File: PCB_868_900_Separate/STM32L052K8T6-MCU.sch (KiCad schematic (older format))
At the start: 27 parts, among them J2 20021121-00010C4LF, J3 B4B-PH-K-S(LF)(SN), J5 0475890001-MicroUSBPort, P1 CONN_02X03, SW2 B3U-1000P, U3 STM32L052C8T6, X3 ABM10-166-12.000MHZ-T3

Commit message: License added and dedicated PA/LNA Match
Working on the separate PA/LNA match version. also added cern license
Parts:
- removed J3: B4B-PH-K-S(LF)(SN), PCB_Footprints:B4B-PH-K-S(LF)(SN), symbol B4B-PH-K-S(LF)(SN)
- removed P1: CONN_02X03, Pin_Headers:Pin_Header_Straight_2x03, symbol CONN_02X03
- added P1: CONN_02X08, Pin_Headers:Pin_Header_Straight_2x08, symbol CONN_02X08
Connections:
- net labels added: PSU_IN, VIN
- wire segments 74 -> 76
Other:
- moved on the sheet: LED2, LED3, R7, R8

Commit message: PCBs Tweaked A lot
PCBs have been tweaked. The separate implementation has been finished
but also has GPIOs from the MCU broken out to the connector, same for
the combined implementation. Both boards now have power indication LEDs
(red).
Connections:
- net labels added: GPIO_PA8, GPIO_PB0, GPIO_PB1, GPIO_PB10, GPIO_PB11, GPIO_PB2
- wire segments 76 -> 88
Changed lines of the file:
@@
 $EndComp
 $Comp
-L GND #PWR30
+L GND #PWR32
 U 1 1 582190B8
 P 1400 5050
-F 0 "#PWR30" H 1400 4800 50  0001 C CNN
+F 0 "#PWR32" H 1400 4800 50  0001 C CNN
 F 1 "GND" H 1405 4877 50  0000 C CNN
 F 2 "" H 1400 5050 50  0000 C CNN
@@
 $EndComp
 $Comp
-L GND #PWR40
+L GND #PWR42
 U 1 1 58219186
 P 4750 5800
-F 0 "#PWR40" H 4750 5550 50  0001 C CNN
+F 0 "#PWR42" H 4750 5550 50  0001 C CNN
 F 1 "GND" H 4755 5627 50  0000 C CNN
 F 2 "" H 4750 5800 50  0000 C CNN
@@
 $EndComp
 $Comp
-L +3.3V #PWR29
+L +3.3V #PWR31
 U 1 1 58219330
 P 1400 4000
-F 0 "#PWR29" H 1400 3850 50  0001 C CNN
+F 0 "#PWR31" H 1400 3850 50  0001 C CNN
 F 1 "+3.3V" H 1415 4173 50  0000 C CNN
 F 2 "" H 1400 4000 50  0000 C CNN
@@
 $EndComp
 $Comp
-L GND #PWR38
+L GND #PWR40
 U 1 1 58219BE3
 P 3450 2950
-F 0 "#PWR38" H 3450 2700 50  0001 C CNN
+F 0 "#PWR40" H 3450 2700 50  0001 C CNN
 F 1 "GND" H 3455 2777 50  0000 C CNN
 F 2 "" H 3450 2950 50  0000 C CNN
@@
 $EndComp
 $Comp
-L +3.3V #PWR36
+L +3.3V #PWR38
 U 1 1 58219CF5
 P 3100 2500
-F 0 "#PWR36" H 3100 2350 50  0001 C CNN
+F 0 "#PWR38" H 3100 2350 50  0001 C CNN
 F 1 "+3.3V" H 3115 2673 50  0000 C CNN
 F 2 "" H 3100 2500 50  0000 C CNN
@@
 $EndComp
 $Comp
-L GND #PWR34
+L GND #PWR36
 U 1 1 5821A196
 P 1700 2950
-F 0 "#PWR34" H 1700 2700 50  0001 C CNN
+F 0 "#PWR36" H 1700 2700 50  0001 C CNN
 F 1 "GND" H 1705 2777 50  0000 C CNN
 F 2 "" H 1700 2950 50  0000 C CNN
@@
 $EndComp
 $Comp
-L GND #PWR35
+L GND #PWR37
 U 1 1 5821A1E0
 P 2500 2950
-F 0 "#PWR35" H 2500 2700 50  0001 C CNN
+F 0 "#PWR37" H 2500 2700 50  0001 C CNN
 F 1 "GND" H 2505 2777 50  0000 C CNN
 F 2 "" H 2500 2950 50  0000 C CNN
@@
 $EndComp
 $Comp
-L +3.3V #PWR33
+L +3.3V #PWR35
 U 1 1 5821A692
 P 1500 2500
-F 0 "#PWR33" H 1500 2350 50  0001 C CNN
+F 0 "#PWR35" H 1500 2350 50  0001 C CNN
 F 1 "+3.3V" H 1515 2673 50  0000 C CNN
 F 2 "" H 1500 2500 50  0000 C CNN
@@
 $EndComp
 $Comp
-L GND #PWR46
+L GND #PWR48
 U 1 1 58221381
 P 9975 3900
-F 0 "#PWR46" H 9975 3650 50  0001 C CNN
+F 0 "#PWR48" H 9975 3650 50  0001 C CNN
 F 1 "GND" H 9980 3727 50  0000 C CNN
 F 2 "" H 9975 3900 50  0000 C CNN
@@
 $EndComp
 $Comp
-L GND #PWR48
+L GND #PWR50
 U 1 1 58221B76
 P 10475 4775
-F 0 "#PWR48" H 10475 4525 50  0001 C CNN
+F 0 "#PWR50" H 10475 4525 50  0001 C CNN
 F 1 "GND" H 10480 4602 50  0000 C CNN
 F 2 "" H 10475 4775 50  0000 C CNN
@@
 $EndComp
 $Comp
-L GND #PWR45
+L GND #PWR47
 U 1 1 58223B2D
 P 9600 4775
-F 0 "#PWR45" H 9600 4525 50  0001 C CNN
+F 0 "#PWR47" H 9600 4525 50  0001 C CNN
 F 1 "GND" H 9605 4602 50  0000 C CNN
 F 2 "" H 9600 4775 50  0000 C CNN
@@
 $EndComp
 $Comp
-L GND #PWR44
+L GND #PWR46
 U 1 1 58224185
 P 9050 4375
-F 0 "#PWR44" H 9050 4125 50  0001 C CNN
+F 0 "#PWR46" H 9050 4125 50  0001 C CNN
 F 1 "GND" H 9055 4202 50  0000 C CNN
 F 2 "" H 9050 4375 50  0000 C CNN
@@
 $EndComp
 $Comp
-L GND #PWR47
+L GND #PWR49
 U 1 1 58224D2B
 P 10425 3125
-F 0 "#PWR47" H 10425 2875 50  0001 C CNN
+F 0 "#PWR49" H 10425 2875 50  0001 C CNN
 F 1 "GND" H 10430 2952 50  0000 C CNN
 F 2 "" H 10425 3125 50  0000 C CNN
@@
 U 1 1 58226A3F
 P 7900 5750
-F 0 "LED2" V 7800 4775 60  0000 L CNN
-F 1 "LTST-C193TBKT-5A" V 7900 4775 60  0000 L CNN
+F 0 "LED2" V 7950 4700 60  0000 L CNN
+F 1 "LTST-C193TBKT-5A" V 8050 4700 60  0000 L CNN
 F 2 "PCB_Footprints:LED0603" H 9325 7675 60  0001 C CNN
 F 3 "http://optoelectronics.liteon.com/upload/download/DS22-2004-060/P_100_LTST-C193TBKT-5A.pdf" H 9525 7800 60  0001 C CNN
@@
 NRST
 $Comp
-L GND #PWR32
+L GND #PWR34
 U 1 1 5824BA14
 P 1400 6250
-F 0 "#PWR32" H 1400 6000 50  0001 C CNN
+F 0 "#PWR34" H 1400 6000 50  0001 C CNN
 F 1 "GND" H 1405 6077 50  0000 C CNN
 F 2 "" H 1400 6250 50  0000 C CNN
@@
 $EndComp
 $Comp
-L +3.3V #PWR31
+L +3.3V #PWR33
 U 1 1 5824BBC1
 P 1400 5575
-F 0 "#PWR31" H 1400 5425 50  0001 C CNN
+F 0 "#PWR33" H 1400 5425 50  0001 C CNN
 F 1 "+3.3V" H 1415 5748 50  0000 C CNN
 F 2 "" H 1400 5575 50  0000 C CNN
@@
 $EndComp
 $Comp
-L GND #PWR43
+L GND #PWR45
 U 1 1 58250111
 P 8025 6000
-F 0 "#PWR43" H 8025 5750 50  0001 C CNN
+F 0 "#PWR45" H 8025 5750 50  0001 C CNN
 F 1 "GND" H 8030 5827 50  0000 C CNN
 F 2 "" H 8025 6000 50  0000 C CNN
@@
 $EndComp
 $Comp
-L GND #PWR39
+L GND #PWR41
 U 1 1 582650D6
 P 4150 4375
-F 0 "#PWR39" H 4150 4125 50  0001 C CNN
+F 0 "#PWR41" H 4150 4125 50  0001 C CNN
 F 1 "GND" H 4155 4202 50  0000 C CNN
 F 2 "" H 4150 4375 50  0000 C CNN
@@
 Connection ~ 3250 4200
 $Comp
-L GND #PWR37
+L GND #PWR39
 U 1 1 58299A73
 P 3125 4200
-F 0 "#PWR37" H 3125 3950 50  0001 C CNN
+F 0 "#PWR39" H 3125 3950 50  0001 C CNN
 F 1 "GND" H 3130 4027 50  0000 C CNN
 F 2 "" H 3125 4200 50  0000 C CNN
@@
 F 3 "" H 5575 5625 50  0000 C CNN
 	1    5575 6825
-	1    0    0    -1
-$EndComp
-Text Label 6000 6975 0    60   ~ 0
+	-1   0    0    1
+$EndComp
+Text Label 5900 6975 0    60   ~ 0
 USART1_TX
-Text Label 6000 6875 0    60   ~ 0
+Text Label 4850 6975 0    60   ~ 0
 USART1_RX
 Wire Wire Line
 	5825 6975 6625 6975
 Wire Wire Line
-	5825 6875 6625 6875
-Text Label 5950 6775 0    60   ~ 0
+	4525 6975 5325 6975
+Text Label 4850 6575 0    60   ~ 0
 SPI2_MOSI
-Text Label 5925 6675 0    60   ~ 0
+Text Label 5875 6575 0    60   ~ 0
 SPI2_MISO
-Text Label 5925 6575 0    60   ~ 0
+Text Label 4850 6475 0    60   ~ 0
 SPI2_SCLK
-Text Label 5925 6475 0    60   ~ 0
+Text Label 5875 6475 0    60   ~ 0
 SPI2_NSS
 Wire Wire Line
-	6400 6775 5825 6775
+	5325 6575 4750 6575
+Wire Wire Line
+	4750 6475 5325 6475
+Wire Wire Line
+	5825 6475 6400 6475
 Wire Wire Line
 	5825 6575 6400 6575
-Wire Wire Line
-	5825 6475 6400 6475
-Wire Wire Line
-	5825 6675 6400 6675
 Text HLabel 10975 5250 2    60   Input ~ 0
 VIN
@@
 Text Label 10300 5250 0    60   ~ 0
 PSU_IN
-Text Label 5950 7075 0    60   ~ 0
+Text Label 5000 7175 0    60   ~ 0
 PSU_IN
 Wire Wire Line
-	6400 7075 5825 7075
-$Comp
-L GND #PWR42
+	5325 7175 4750 7175
+$Comp
+L GND #PWR44
 U 1 1 58246BF1
 P 5825 7175
-F 0 "#PWR42" H 5825 6925 50  0001 C CNN
+F 0 "#PWR44" H 5825 6925 50  0001 C CNN
 F 1 "GND" H 5830 7002 50  0000 C CNN
 F 2 "" H 5825 7175 50  0000 C CNN
@@
 $EndComp
 $Comp
-L GND #PWR41
+L GND #PWR43
 U 1 1 5824B1D0
-P 5325 7175
-F 0 "#PWR41" H 5325 6925 50  0001 C CNN
-F 1 "GND" H 5330 7002 50  0000 C CNN
-F 2 "" H 5325 7175 50  0000 C CNN
-F 3 "" H 5325 7175 50  0000 C CNN
-	1    5325 7175
-	1    0    0    -1
-$EndComp
+P 4700 7400
+F 0 "#PWR43" H 4700 7150 50  0001 C CNN
+F 1 "GND" H 4705 7227 50  0000 C CNN
+F 2 "" H 4700 7400 50  0000 C CNN
+F 3 "" H 4700 7400 50  0000 C CNN
+	1    4700 7400
+	1    0    0    -1
+$EndComp
+Text Label 6500 4200 0    60   ~ 0
+GPIO_PB0
+Text Label 6500 4300 0    60   ~ 0
+GPIO_PB1
+Text Label 6500 4400 0    60   ~ 0
+GPIO_PB2
+Text Label 6500 5200 0    60   ~ 0
+GPIO_PB10
+Text Label 6500 5300 0    60   ~ 0
+GPIO_PB11
+Wire Wire Line
+	7050 5200 6500 5200
+Wire Wire Line
+	7050 5300 6500 5300
+Wire Wire Line
+	7025 4400 6500 4400
+Wire Wire Line
+	7025 4300 6500 4300
+Wire Wire Line
+	7025 4200 6500 4200
+Text Label 5875 6675 0    60   ~ 0
+GPIO_PB0
+Text Label 4850 6675 0    60   ~ 0
+GPIO_PB1
+Text Label 5875 6775 0    60   ~ 0
+GPIO_PB2
+Wire Wire Line
+	6350 6775 5825 6775
+Wire Wire Line
+	5325 6675 4800 6675
+Wire Wire Line
+	6350 6675 5825 6675
+Text Label 4850 6775 0    60   ~ 0
+GPIO_PB10
+Text Label 5875 6875 0    60   ~ 0
+GPIO_PB11
+Wire Wire Line
+	5325 6775 4775 6775
+Wire Wire Line
+	6375 6875 5825 6875
+Wire Wire Line
+	6500 3300 7225 3300
+Text Label 6650 3300 0    60   ~ 0
+GPIO_PA8
+Text Label 4850 6875 0    60   ~ 0
+GPIO_PA8
+Wire Wire Line
+	5325 6875 4775 6875
 $EndSCHEMATC

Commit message: Additional GPIO
Two additional GPIO pins from the STM32L0 have been added to the
connector, now there is a signal on every pin. The connector component
has been replaced with one that has a STEP 3D model for proper 3D model
exporting from KiCAD for enclosure design. This has been done to both
versions of the radio.
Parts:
- removed P1: CONN_02X08, Pin_Headers:Pin_Header_Straight_2x08, symbol CONN_02X08
- added P1: 61301621121, PCB_Footprints:61301621121, symbol 61301621121
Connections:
- net labels added: GPIO_PA15, GPIO_PB3
- wire segments 88 -> 92
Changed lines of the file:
@@
 $EndComp
 $Comp
-L GND #PWR33
+L GND #PWR032
 U 1 1 582190B8
 P 1400 5050
-F 0 "#PWR33" H 1400 4800 50  0001 C CNN
+F 0 "#PWR032" H 1400 4800 50  0001 C CNN
 F 1 "GND" H 1405 4877 50  0000 C CNN
 F 2 "" H 1400 5050 50  0000 C CNN
@@
 $EndComp
 $Comp
-L GND #PWR44
+L GND #PWR033
 U 1 1 58219186
 P 4750 5800
-F 0 "#PWR44" H 4750 5550 50  0001 C CNN
+F 0 "#PWR033" H 4750 5550 50  0001 C CNN
 F 1 "GND" H 4755 5627 50  0000 C CNN
 F 2 "" H 4750 5800 50  0000 C CNN
@@
 $EndComp
 $Comp
-L +3.3V #PWR32
+L +3.3V #PWR034
 U 1 1 58219330
 P 1400 4000
-F 0 "#PWR32" H 1400 3850 50  0001 C CNN
+F 0 "#PWR034" H 1400 3850 50  0001 C CNN
 F 1 "+3.3V" H 1415 4173 50  0000 C CNN
 F 2 "" H 1400 4000 50  0000 C CNN
@@
 $EndComp
 $Comp
-L GND #PWR41
+L GND #PWR035
 U 1 1 58219BE3
 P 3450 2950
-F 0 "#PWR41" H 3450 2700 50  0001 C CNN
+F 0 "#PWR035" H 3450 2700 50  0001 C CNN
 F 1 "GND" H 3455 2777 50  0000 C CNN
 F 2 "" H 3450 2950 50  0000 C CNN
@@
 $EndComp
 $Comp
-L +3.3V #PWR39
+L +3.3V #PWR036
 U 1 1 58219CF5
 P 3100 2500
-F 0 "#PWR39" H 3100 2350 50  0001 C CNN
+F 0 "#PWR036" H 3100 2350 50  0001 C CNN
 F 1 "+3.3V" H 3115 2673 50  0000 C CNN
 F 2 "" H 3100 2500 50  0000 C CNN
@@
 $EndComp
 $Comp
-L GND #PWR37
+L GND #PWR037
 U 1 1 5821A196
 P 1700 2950
-F 0 "#PWR37" H 1700 2700 50  0001 C CNN
+F 0 "#PWR037" H 1700 2700 50  0001 C CNN
 F 1 "GND" H 1705 2777 50  0000 C CNN
 F 2 "" H 1700 2950 50  0000 C CNN
@@
 $EndComp
 $Comp
-L GND #PWR38
+L GND #PWR038
 U 1 1 5821A1E0
 P 2500 2950
-F 0 "#PWR38" H 2500 2700 50  0001 C CNN
+F 0 "#PWR038" H 2500 2700 50  0001 C CNN
 F 1 "GND" H 2505 2777 50  0000 C CNN
 F 2 "" H 2500 2950 50  0000 C CNN
@@
 $EndComp
 $Comp
-L +3.3V #PWR36
+L +3.3V #PWR039
 U 1 1 5821A692
 P 1500 2500
-F 0 "#PWR36" H 1500 2350 50  0001 C CNN
+F 0 "#PWR039" H 1500 2350 50  0001 C CNN
 F 1 "+3.3V" H 1515 2673 50  0000 C CNN
 F 2 "" H 1500 2500 50  0000 C CNN
@@
 $EndComp
 $Comp
-L GND #PWR49
+L GND #PWR040
 U 1 1 58221381
 P 9975 3900
-F 0 "#PWR49" H 9975 3650 50  0001 C CNN
+F 0 "#PWR040" H 9975 3650 50  0001 C CNN
 F 1 "GND" H 9980 3727 50  0000 C CNN
 F 2 "" H 9975 3900 50  0000 C CNN
@@
 $EndComp
 $Comp
-L GND #PWR51
+L GND #PWR041
 U 1 1 58221B76
 P 10475 4775
-F 0 "#PWR51" H 10475 4525 50  0001 C CNN
+F 0 "#PWR041" H 10475 4525 50  0001 C CNN
 F 1 "GND" H 10480 4602 50  0000 C CNN
 F 2 "" H 10475 4775 50  0000 C CNN
@@
 $EndComp
 $Comp
-L GND #PWR48
+L GND #PWR042
 U 1 1 58223B2D
 P 9600 4775
-F 0 "#PWR48" H 9600 4525 50  0001 C CNN
+F 0 "#PWR042" H 9600 4525 50  0001 C CNN
 F 1 "GND" H 9605 4602 50  0000 C CNN
 F 2 "" H 9600 4775 50  0000 C CNN
@@
 $EndComp
 $Comp
-L GND #PWR47
+L GND #PWR043
 U 1 1 58224185
 P 9050 4375
-F 0 "#PWR47" H 9050 4125 50  0001 C CNN
+F 0 "#PWR043" H 9050 4125 50  0001 C CNN
 F 1 "GND" H 9055 4202 50  0000 C CNN
 F 2 "" H 9050 4375 50  0000 C CNN
@@
 $EndComp
 $Comp
-L GND #PWR50
+L GND #PWR044
 U 1 1 58224D2B
 P 10425 3125
-F 0 "#PWR50" H 10425 2875 50  0001 C CNN
+F 0 "#PWR044" H 10425 2875 50  0001 C CNN
 F 1 "GND" H 10430 2952 50  0000 C CNN
 F 2 "" H 10425 3125 50  0000 C CNN
@@
 NRST
 $Comp
-L GND #PWR35
+L GND #PWR045
 U 1 1 5824BA14
 P 1400 6250
-F 0 "#PWR35" H 1400 6000 50  0001 C CNN
+F 0 "#PWR045" H 1400 6000 50  0001 C CNN
 F 1 "GND" H 1405 6077 50  0000 C CNN
 F 2 "" H 1400 6250 50  0000 C CNN
@@
 $EndComp
 $Comp
-L +3.3V #PWR34
+L +3.3V #PWR046
 U 1 1 5824BBC1
 P 1400 5575
-F 0 "#PWR34" H 1400 5425 50  0001 C CNN
+F 0 "#PWR046" H 1400 5425 50  0001 C CNN
 F 1 "+3.3V" H 1415 5748 50  0000 C CNN
 F 2 "" H 1400 5575 50  0000 C CNN
@@
 $EndComp
 $Comp
-L GND #PWR46
+L GND #PWR047
 U 1 1 58250111
 P 8025 6000
-F 0 "#PWR46" H 8025 5750 50  0001 C CNN
+F 0 "#PWR047" H 8025 5750 50  0001 C CNN
 F 1 "GND" H 8030 5827 50  0000 C CNN
 F 2 "" H 8025 6000 50  0000 C CNN
@@
 $EndComp
 $Comp
-L GND #PWR42
+L GND #PWR048
 U 1 1 582650D6
 P 4150 4375
-F 0 "#PWR42" H 4150 4125 50  0001 C CNN
+F 0 "#PWR048" H 4150 4125 50  0001 C CNN
 F 1 "GND" H 4155 4202 50  0000 C CNN
 F 2 "" H 4150 4375 50  0000 C CNN
@@
 Connection ~ 3250 4200
 $Comp
-L GND #PWR40
+L GND #PWR049
 U 1 1 58299A73
 P 3125 4200
-F 0 "#PWR40" H 3125 3950 50  0001 C CNN
+F 0 "#PWR049" H 3125 3950 50  0001 C CNN
 F 1 "GND" H 3130 4027 50  0000 C CNN
 F 2 "" H 3125 4200 50  0000 C CNN
@@
 $EndComp
 Connection ~ 3125 4200
-$Comp
-L CONN_02X08 P1
-U 1 1 5823F6D4
-P 5575 6825
-F 0 "P1" H 5575 7390 50  0000 C CNN
-F 1 "CONN_02X08" H 5575 7299 50  0000 C CNN
-F 2 "Pin_Headers:Pin_Header_Straight_2x08" H 5575 5625 50  0001 C CNN
-F 3 "" H 5575 5625 50  0000 C CNN
-	1    5575 6825
-	-1   0    0    1
-$EndComp
-Text Label 5900 6975 0    60   ~ 0
+Text Label 6000 6975 0    60   ~ 0
 USART1_TX
 Text Label 4850 6975 0    60   ~ 0
 USART1_RX
 Wire Wire Line
-	5825 6975 6625 6975
+	5925 6975 6725 6975
 Wire Wire Line
 	4525 6975 5325 6975
 Text Label 4850 6575 0    60   ~ 0
 SPI2_MOSI
-Text Label 5875 6575 0    60   ~ 0
+Text Label 5975 6575 0    60   ~ 0
 SPI2_MISO
 Text Label 4850 6475 0    60   ~ 0
 SPI2_SCLK
-Text Label 5875 6475 0    60   ~ 0
+Text Label 5975 6475 0    60   ~ 0
 SPI2_NSS
 Wire Wire Line
@@
 	4750 6475 5325 6475
 Wire Wire Line
-	5825 6475 6400 6475
-Wire Wire Line
-	5825 6575 6400 6575
+	5925 6475 6500 6475
+Wire Wire Line
+	5925 6575 6500 6575
 Text HLabel 10975 5250 2    60   Input ~ 0
 VIN
@@
 	5325 7175 4750 7175
 $Comp
-L GND #PWR45
+L GND #PWR050
 U 1 1 58246BF1
-P 5825 7175
-F 0 "#PWR45" H 5825 6925 50  0001 C CNN
-F 1 "GND" H 5830 7002 50  0000 C CNN
-F 2 "" H 5825 7175 50  0000 C CNN
-F 3 "" H 5825 7175 50  0000 C CNN
-	1    5825 7175
-	1    0    0    -1
-$EndComp
-$Comp
-L GND #PWR43
+P 5925 7175
+F 0 "#PWR050" H 5925 6925 50  0001 C CNN
+F 1 "GND" H 5930 7002 50  0000 C CNN
+F 2 "" H 5925 7175 50  0000 C CNN
+F 3 "" H 5925 7175 50  0000 C CNN
+	1    5925 7175
+	1    0    0    -1
+$EndComp
+$Comp
+L GND #PWR051
 U 1 1 5824B1D0
 P 4700 7400
-F 0 "#PWR43" H 4700 7150 50  0001 C CNN
+F 0 "#PWR051" H 4700 7150 50  0001 C CNN
 F 1 "GND" H 4705 7227 50  0000 C CNN
 F 2 "" H 4700 7400 50  0000 C CNN
@@
 Wire Wire Line
 	7025 4200 6500 4200
-Text Label 5875 6675 0    60   ~ 0
+Text Label 5975 6675 0    60   ~ 0
 GPIO_PB0
 Text Label 4850 6675 0    60   ~ 0
 GPIO_PB1
-Text Label 5875 6775 0    60   ~ 0
+Text Label 5975 6775 0    60   ~ 0
 GPIO_PB2
 Wire Wire Line
-	6350 6775 5825 6775
+	6450 6775 5925 6775
 Wire Wire Line
 	5325 6675 4800 6675
 Wire Wire Line
-	6350 6675 5825 6675
+	6450 6675 5925 6675
 Text Label 4850 6775 0    60   ~ 0
 GPIO_PB10
-Text Label 5875 6875 0    60   ~ 0
+Text Label 5975 6875 0    60   ~ 0
 GPIO_PB11
 Wire Wire Line
 	5325 6775 4775 6775
 Wire Wire Line
-	6375 6875 5825 6875
+	6475 6875 5925 6875
 Wire Wire Line
 	6500 3300 7225 3300
@@
 Wire Wire Line
 	5325 6875 4775 6875
+$Comp
+L 61301621121 P1
+U 1 1 582B02E0
+P 5525 7075
+F 0 "P1" H 5425 6238 60  0000 C CNN
+F 1 "61301621121" H 5425 6344 60  0000 C CNN
+F 2 "PCB_Footprints:61301621121" H 5675 7375 60  0001 C CNN
+F 3 "http://katalog.we-online.de/em/datasheet/6130xx21121.pdf" H 5250 7450 60  0001 C CNN
+F 4 "0.71280 @ 500" H 5350 7550 60  0001 C CNN "Cost"
+F 5 "14 Nov 2016" H 5450 7650 60  0001 C CNN "Date Created "
+F 6 "14 Nov 2016" H 5550 7750 60  0001 C CNN "Date Modified"
+F 7 "Adam Vadala-Roth" H 5650 7850 60  0001 C CNN "Designer "
+F 8 "8.54mm" H 5750 7950 60  0001 C CNN "Height"
+F 9 "Yes" H 5850 8050 60  0001 C CNN "RHoS?"
+F 10 "Wurth Electronics Inc" H 5950 8150 60  0001 C CNN "MFR"
+F 11 "B3B-PH-SM4-TB(LF)(SN)" H 6050 8250 60  0001 C CNN "MFR#"
+F 12 "SMT/SMD" H 6150 8350 60  0001 C CNN "Mounting"
+F 13 "16" H 6250 8450 60  0001 C CNN "Pin Count#"
+F 14 "Active" H 6350 8550 60  0001 C CNN "Status"
+F 15 "N/A" H 6450 8650 60  0001 C CNN "Tolerance"
+F 16 "Throughhole Pin Header 2.54mm Pitch" H 6550 8750 60  0001 C CNN "Type"
+F 17 "N/A" H 6650 8850 60  0001 C CNN "Voltage"
+F 18 "N/A" H 6750 8950 60  0001 C CNN "Wattage"
+F 19 "N/A" H 6850 9050 60  0001 C CNN "Component-Value"
+F 20 "16 Positions Header, Unshrouded Connector 0.100\" (2.54mm) Through Hole Gold" H 6950 9150 60  0001 C CNN "Description"
+	1    5525 7075
+	-1   0    0    1
+$EndComp
+Text Label 5925 7075 0    60   ~ 0
+GPIO_PA15
+Text Label 4875 7075 0    60   ~ 0
+GPIO_PB3
+Text Label 6500 4000 0    60   ~ 0
+GPIO_PA15
+Text Label 6500 4500 0    60   ~ 0
+GPIO_PB3
+Wire Wire Line
+	7025 4500 6500 4500
+Wire Wire Line
+	7025 4000 6500 4000
+Wire Wire Line
+	4525 7075 5325 7075
+Wire Wire Line
+	5925 7075 6725 7075
 $EndSCHEMATC

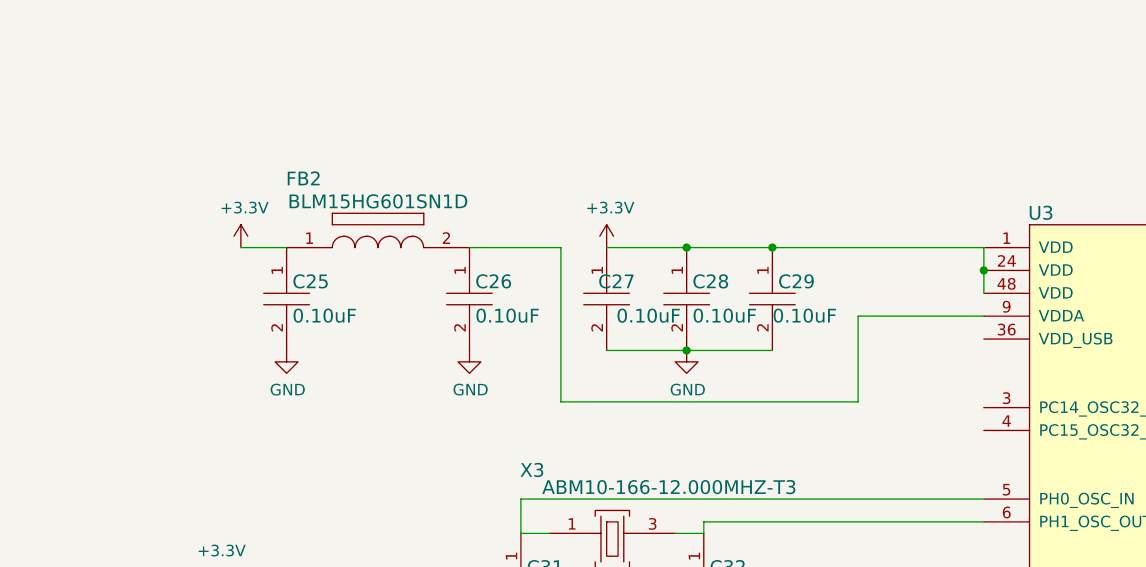
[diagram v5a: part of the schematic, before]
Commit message: USB VDD
Found schematic bug, USB VDD was not tied to 3V3 supply or applied a
bypass cap, this has been resolved in both implementations of the S1G.
STM32L0 program manual added to the datasheets collection for the
project. Schematic PDFs updated.
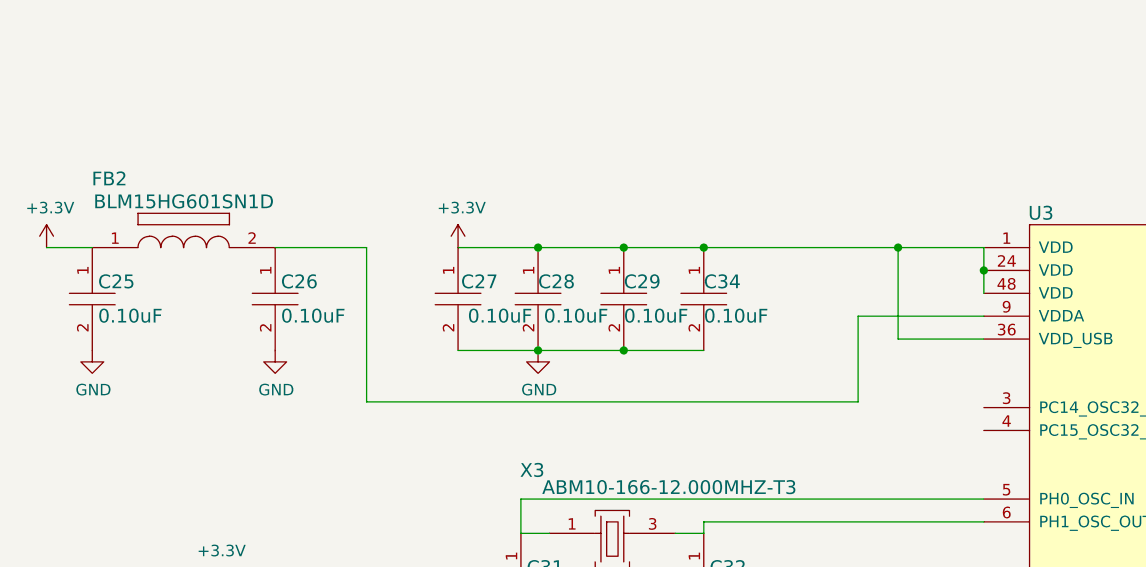
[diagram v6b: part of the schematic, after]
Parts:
- added C34: CL05B104JP5NNNC, PCB_Footprints:C0402, symbol CL05B104JP5NNNC
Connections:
- wire segments 92 -> 94
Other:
- moved on the sheet: C25, C26, C27, C28, C29, FB2
